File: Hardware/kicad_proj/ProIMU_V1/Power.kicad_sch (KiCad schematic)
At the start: 12 parts

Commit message: Update: Schematic
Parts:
- added SW?: SW_SPDT, symbol Switch:SW_SPDT
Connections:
- net GND: now also SW?.3 (C)
- net 3.3V renamed +3V3
- net 5V renamed +5V
- net EN: no longer names the net of U?.5 (EN), U?.5 (EN)
- net EN: now also SW?.1 (A)
- net Vin renamed VDD
- net VDD: now also SW?.2 (B)
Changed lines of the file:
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@@
   (junction (at 166.37 142.24) (diameter 0) (color 0 0 0 0)
   )
+  (junction (at 76.2 87.63) (diameter 0) (color 0 0 0 0)
+  )
   (junction (at 168.91 121.92) (diameter 0) (color 0 0 0 0)
   )
@@
     (stroke (width 0) (type default) (color 0 0 0 0))
   )
-  (wire (pts (xy 93.98 62.23) (xy 111.76 62.23))
-    (stroke (width 0) (type default) (color 0 0 0 0))
-  )
   (wire (pts (xy 166.37 142.24) (xy 166.37 144.78))
     (stroke (width 0) (type default) (color 0 0 0 0))
@@
     (stroke (width 0) (type default) (color 0 0 0 0))
   )
+  (wire (pts (xy 43.18 96.52) (xy 38.1 96.52))
+    (stroke (width 0) (type default) (color 0 0 0 0))
+  )
   (wire (pts (xy 162.56 73.66) (xy 162.56 76.2))
     (stroke (width 0) (type default) (color 0 0 0 0))
@@
     (stroke (width 0) (type default) (color 0 0 0 0))
   )
-  (wire (pts (xy 93.98 67.31) (xy 111.76 67.31))
+  (wire (pts (xy 76.2 87.63) (xy 58.42 87.63))
     (stroke (width 0) (type default) (color 0 0 0 0))
   )
@@
     (stroke (width 0) (type default) (color 0 0 0 0))
   )
+  (wire (pts (xy 99.06 67.31) (xy 111.76 67.31))
+    (stroke (width 0) (type default) (color 0 0 0 0))
+  )
+  (wire (pts (xy 38.1 96.52) (xy 38.1 92.71))
+    (stroke (width 0) (type default) (color 0 0 0 0))
+  )
   (wire (pts (xy 134.62 62.23) (xy 134.62 55.88))
     (stroke (width 0) (type default) (color 0 0 0 0))
@@
     (stroke (width 0) (type default) (color 0 0 0 0))
   )
+  (wire (pts (xy 58.42 99.06) (xy 58.42 101.6))
+    (stroke (width 0) (type default) (color 0 0 0 0))
+  )
   (wire (pts (xy 123.19 129.54) (xy 123.19 133.35))
     (stroke (width 0) (type default) (color 0 0 0 0))
   )
+  (wire (pts (xy 96.52 62.23) (xy 111.76 62.23))
+    (stroke (width 0) (type default) (color 0 0 0 0))
+  )
   (wire (pts (xy 133.35 124.46) (xy 146.05 124.46))
     (stroke (width 0) (type default) (color 0 0 0 0))
@@
     (stroke (width 0) (type default) (color 0 0 0 0))
   )
-  (wire (pts (xy 95.25 124.46) (xy 113.03 124.46))
+  (wire (pts (xy 184.15 60.96) (xy 184.15 64.77))
+    (stroke (width 0) (type default) (color 0 0 0 0))
+  )
+  (wire (pts (xy 95.25 113.03) (xy 95.25 119.38))
+    (stroke (width 0) (type default) (color 0 0 0 0))
+  )
+  (wire (pts (xy 76.2 124.46) (xy 113.03 124.46))
     (stroke (width 0) (type default) (color 0 0 0 0))
   )
@@
     (stroke (width 0) (type default) (color 0 0 0 0))
   )
+  (wire (pts (xy 58.42 87.63) (xy 58.42 93.98))
+    (stroke (width 0) (type default) (color 0 0 0 0))
+  )
   (wire (pts (xy 134.62 55.88) (xy 139.7 55.88))
     (stroke (width 0) (type default) (color 0 0 0 0))
@@
     (stroke (width 0) (type default) (color 0 0 0 0))
   )
+  (wire (pts (xy 99.06 67.31) (xy 99.06 87.63))
+    (stroke (width 0) (type default) (color 0 0 0 0))
+  )
   (wire (pts (xy 140.97 121.92) (xy 148.59 121.92))
     (stroke (width 0) (type default) (color 0 0 0 0))
@@
     (stroke (width 0) (type default) (color 0 0 0 0))
   )
-  (wire (pts (xy 168.91 121.92) (xy 184.15 121.92))
+  (wire (pts (xy 168.91 121.92) (xy 185.42 121.92))
+    (stroke (width 0) (type default) (color 0 0 0 0))
+  )
+  (wire (pts (xy 76.2 124.46) (xy 76.2 87.63))
     (stroke (width 0) (type default) (color 0 0 0 0))
   )
@@
     (stroke (width 0) (type default) (color 0 0 0 0))
   )
+  (wire (pts (xy 99.06 87.63) (xy 76.2 87.63))
+    (stroke (width 0) (type default) (color 0 0 0 0))
+  )
+  (wire (pts (xy 58.42 93.98) (xy 53.34 93.98))
+    (stroke (width 0) (type default) (color 0 0 0 0))
+  )
+  (wire (pts (xy 96.52 54.61) (xy 96.52 62.23))
+    (stroke (width 0) (type default) (color 0 0 0 0))
+  )
   (wire (pts (xy 162.56 68.58) (xy 162.56 64.77))
     (stroke (width 0) (type default) (color 0 0 0 0))
@@
     (stroke (width 0) (type default) (color 0 0 0 0))
   )
+  (wire (pts (xy 185.42 114.3) (xy 185.42 121.92))
+    (stroke (width 0) (type default) (color 0 0 0 0))
+  )
+  (wire (pts (xy 53.34 99.06) (xy 58.42 99.06))
+    (stroke (width 0) (type default) (color 0 0 0 0))
+  )
   (wire (pts (xy 95.25 119.38) (xy 113.03 119.38))
     (stroke (width 0) (type default) (color 0 0 0 0))
@@
     (stroke (width 0) (type default) (color 0 0 0 0))
   )
-  (wire (pts (xy 167.64 64.77) (xy 182.88 64.77))
-    (stroke (width 0) (type default) (color 0 0 0 0))
-  )
-  (hierarchical_label "Vin" (shape input) (at 93.98 62.23 180)
-    (effects (font (size 1.27 1.27)) (justify right))
-  )
-  (hierarchical_label "3.3V" (shape input) (at 182.88 64.77 0)
-    (effects (font (size 1.27 1.27)) (justify left))
-  )
-  (hierarchical_label "EN" (shape input) (at 95.25 124.46 180)
-    (effects (font (size 1.27 1.27)) (justify right))
-  )
-  (hierarchical_label "EN" (shape input) (at 93.98 67.31 180)
-    (effects (font (size 1.27 1.27)) (justify right))
-  )
-  (hierarchical_label "Vin" (shape input) (at 95.25 119.38 180)
-    (effects (font (size 1.27 1.27)) (justify right))
-  )
-  (hierarchical_label "5V" (shape input) (at 184.15 121.92 0)
-    (effects (font (size 1.27 1.27)) (justify left))
+  (wire (pts (xy 167.64 64.77) (xy 184.15 64.77))
+    (stroke (width 0) (type default) (color 0 0 0 0))
   )
   (symbol (lib_id "pspice:INDUCTOR") (at 153.67 64.77 0) (unit 1)
@@
     (pin "2")
   )
+  (symbol (lib_id "power:VDD") (at 38.1 92.71 0) (unit 1)
+    (in_bom yes) (on_board yes) (fields_autoplaced)
+    (property "Reference" "#PWR?" (id 0) (at 38.1 96.52 0)
+      (effects (font (size 1.27 1.27)) hide)
+    )
+    (property "Value" "VDD" (id 1) (at 38.1 87.63 0))
+    (property "Footprint" "" (id 2) (at 38.1 92.71 0)
+      (effects (font (size 1.27 1.27)) hide)
+    )
+    (property "Datasheet" "" (id 3) (at 38.1 92.71 0)
+      (effects (font (size 1.27 1.27)) hide)
+    )
+    (pin "1")
+  )
   (symbol (lib_id "Device:R_Small") (at 163.83 128.27 0) (mirror x) (unit 1)
     (in_bom yes) (on_board yes)
@@
     (pin "2")
   )
+  (symbol (lib_id "power:+3V3") (at 184.15 60.96 0) (unit 1)
+    (in_bom yes) (on_board yes) (fields_autoplaced)
+    (property "Reference" "#PWR?" (id 0) (at 184.15 64.77 0)
+      (effects (font (size 1.27 1.27)) hide)
+    )
+    (property "Value" "+3V3" (id 1) (at 184.15 55.88 0))
+    (property "Footprint" "" (id 2) (at 184.15 60.96 0)
+      (effects (font (size 1.27 1.27)) hide)
+    )
+    (property "Datasheet" "" (id 3) (at 184.15 60.96 0)
+      (effects (font (size 1.27 1.27)) hide)
+    )
+    (pin "1")
+  )
   (symbol (lib_id "Device:C_Small") (at 167.64 73.66 0) (unit 1)
     (in_bom yes) (on_board yes) (fields_autoplaced)
@@
     (pin "1")
     (pin "2")
+  )
+  (symbol (lib_id "power:GND") (at 58.42 101.6 0) (unit 1)
+    (in_bom yes) (on_board yes) (fields_autoplaced)
+    (property "Reference" "#PWR?" (id 0) (at 58.42 107.95 0)
+      (effects (font (size 1.27 1.27)) hide)
+    )
+    (property "Value" "GND" (id 1) (at 58.42 106.68 0))
+    (property "Footprint" "" (id 2) (at 58.42 101.6 0)
+      (effects (font (size 1.27 1.27)) hide)
+    )
+    (property "Datasheet" "" (id 3) (at 58.42 101.6 0)
+      (effects (font (size 1.27 1.27)) hide)
+    )
+    (pin "1")
   )
   (symbol (lib_id "Device:C_Small") (at 139.7 60.96 0) (unit 1)
@@
     (pin "1")
   )
+  (symbol (lib_id "Switch:SW_SPDT") (at 48.26 96.52 0) (unit 1)
+    (in_bom yes) (on_board yes) (fields_autoplaced)
+    (property "Reference" "SW?" (id 0) (at 48.26 88.9 0))
+    (property "Value" "SW_SPDT" (id 1) (at 48.26 91.44 0))
+    (property "Footprint" "" (id 2) (at 48.26 96.52 0)
+      (effects (font (size 1.27 1.27)) hide)
+    )
+    (property "Datasheet" "~" (id 3) (at 48.26 96.52 0)
+      (effects (font (size 1.27 1.27)) hide)
+    )
+    (pin "1")
+    (pin "2")
+    (pin "3")
+  )
+  (symbol (lib_id "power:VDD") (at 95.25 113.03 0) (unit 1)
+    (in_bom yes) (on_board yes) (fields_autoplaced)
+    (property "Reference" "#PWR?" (id 0) (at 95.25 116.84 0)
+      (effects (font (size 1.27 1.27)) hide)
+    )
+    (property "Value" "VDD" (id 1) (at 95.25 107.95 0))
+    (property "Footprint" "" (id 2) (at 95.25 113.03 0)
+      (effects (font (size 1.27 1.27)) hide)
+    )
+    (property "Datasheet" "" (id 3) (at 95.25 113.03 0)
+      (effects (font (size 1.27 1.27)) hide)
+    )
+    (pin "1")
+  )
   (symbol (lib_id "Device:R_Small") (at 163.83 137.16 0) (mirror x) (unit 1)
     (in_bom yes) (on_board yes)
@@
     (pin "2")
   )
+  (symbol (lib_id "power:VDD") (at 96.52 54.61 0) (unit 1)
+    (in_bom yes) (on_board yes) (fields_autoplaced)
+    (property "Reference" "#PWR?" (id 0) (at 96.52 58.42 0)
+      (effects (font (size 1.27 1.27)) hide)
+    )
+    (property "Value" "VDD" (id 1) (at 96.52 49.53 0))
+    (property "Footprint" "" (id 2) (at 96.52 54.61 0)
+      (effects (font (size 1.27 1.27)) hide)
+    )
+    (property "Datasheet" "" (id 3) (at 96.52 54.61 0)
+      (effects (font (size 1.27 1.27)) hide)
+    )
+    (pin "1")
+  )
   (symbol (lib_id "Device:R_Small") (at 162.56 80.01 0) (mirror x) (unit 1)
     (in_bom yes) (on_board yes)
@@
     (pin "2")
   )
+  (symbol (lib_id "power:+5V") (at 185.42 114.3 0) (unit 1)
+    (in_bom yes) (on_board yes) (fields_autoplaced)
+    (property "Reference" "#PWR?" (id 0) (at 185.42 118.11 0)
+      (effects (font (size 1.27 1.27)) hide)
+    )
+    (property "Value" "+5V" (id 1) (at 185.42 109.22 0))
+    (property "Footprint" "" (id 2) (at 185.42 114.3 0)
+      (effects (font (size 1.27 1.27)) hide)
+    )
+    (property "Datasheet" "" (id 3) (at 185.42 114.3 0)
+      (effects (font (size 1.27 1.27)) hide)
+    )
+    (pin "1")
+  )
   (symbol (lib_id "Regulator_Switching:TPS54308") (at 121.92 64.77 0) (unit 1)

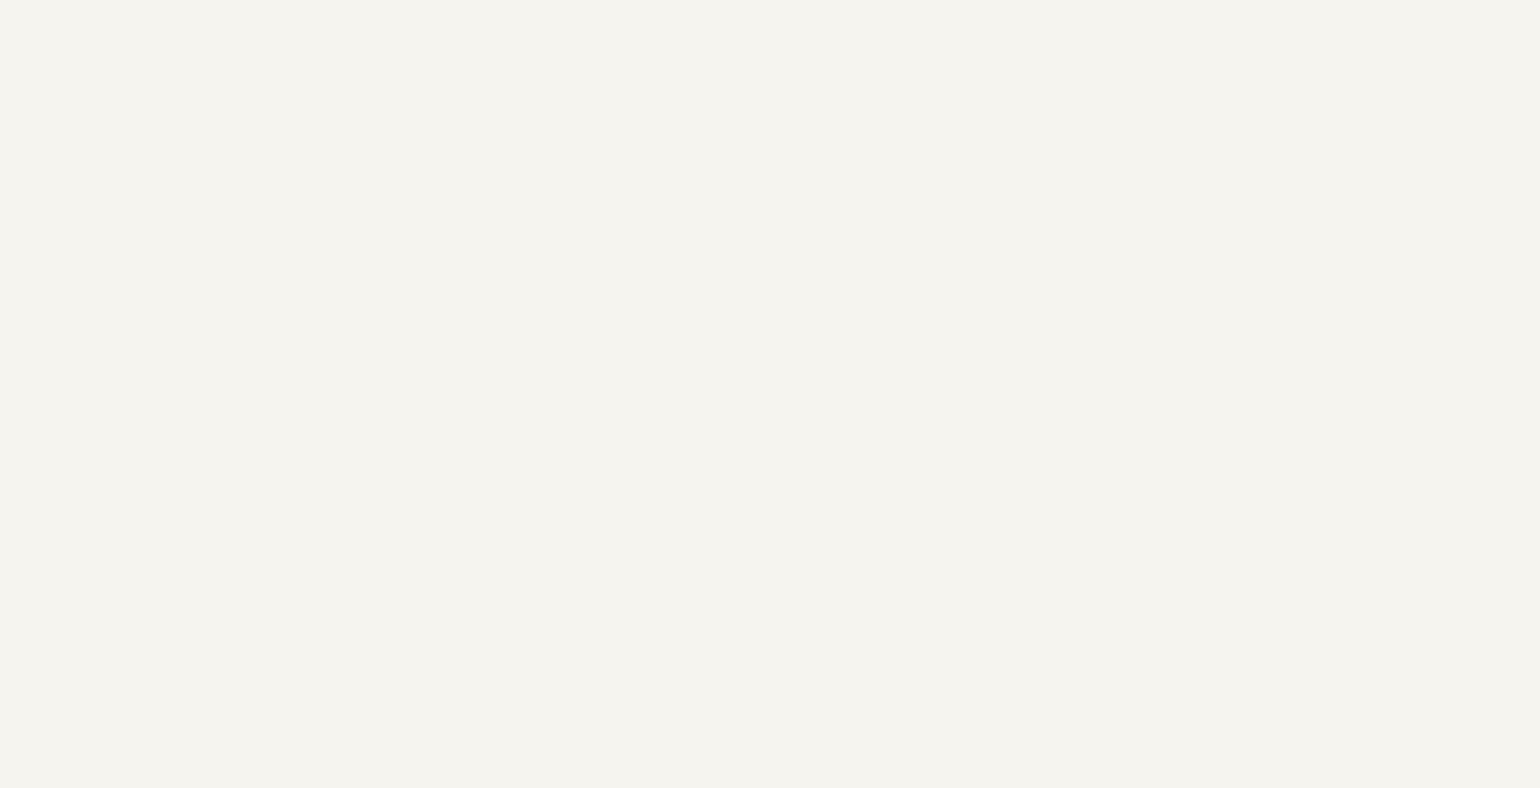
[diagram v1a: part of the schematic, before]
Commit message: Schematic Updated. Removed unecessary schematic pages
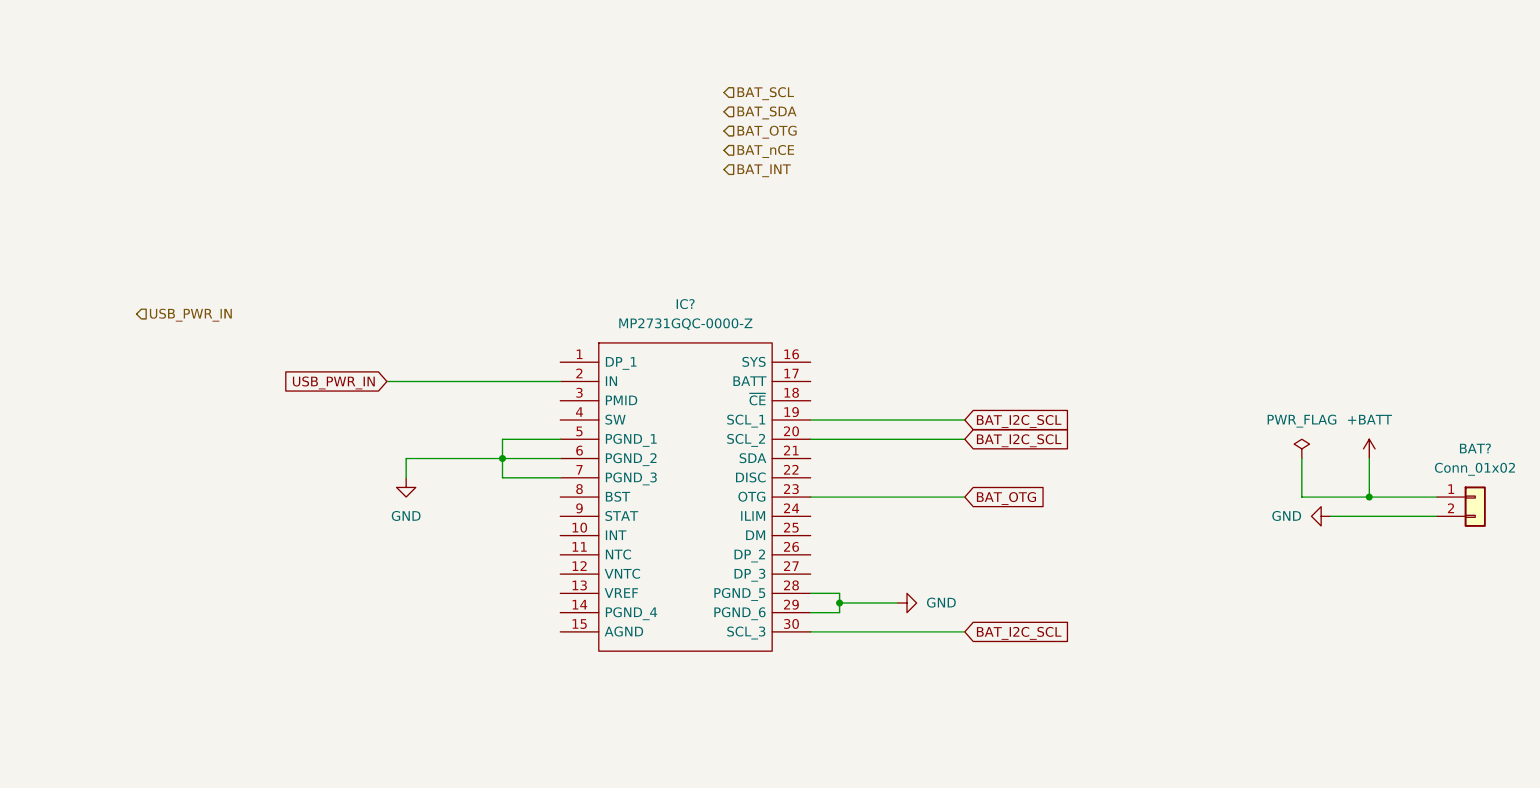
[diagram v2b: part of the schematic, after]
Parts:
- added BAT?: Conn_01x02, Connector_PinSocket_2.54mm:PinSocket_1x02_P2.54mm_Vertical, symbol Connector_Generic:Conn_01x02
- added IC?: MP2731GQC-0000-Z, footprints:MP2731GQC0000Z, symbol MP2731GQC-0000-Z:MP2731GQC-0000-Z
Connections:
- net GND: now also BAT?.2 (Pin_2), IC?.28 (PGND_5), IC?.29 (PGND_6), IC?.5 (PGND_1), IC?.6 (PGND_2), IC?.7 (PGND_3)
- new net +BATT: BAT?.1 (Pin_1)
- new net BAT_I2C_SCL: IC?.19 (SCL_1), IC?.20 (SCL_2), IC?.30 (SCL_3)
- new net BAT_OTG: IC?.23 (OTG)
- new net USB_PWR_IN: IC?.2 (IN)
